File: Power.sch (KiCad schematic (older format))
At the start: 29 parts

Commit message: Clean up, add notes
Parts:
- added C?: 1u, symbol Device:C
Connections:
- net +5V: now also C?.1
- net GND: now also C?.2
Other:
- note added: "6 months sleep: 6*30*24h * (30e-3)mA = 130mAh\n3 days run: 3*24h * 10mA = 720mAh\n\nTotal: 850mAh\nEst. True Total: 500mAh"
- note added: "PS: Pull low for power save mode\nand pull high for fixed switching \nfrequency operation. \n\nEfficiency:\n85% @ 1-3mA PSM\n25% @ 1-3mA FFM\n"
- note added: "Power Consumption Rough Max Estimates"
- note added: "Shutdown Iq: 0.1uA typ, 1uA max\nRun efficiency: 85% (-0.5mA res div)"
- note added: "Shutdown Iq: 0.2uA typ, 1uA max\nRun Iq: 250uA typ, 425uA max @ 250mA"
- note added: "Sleep Total Iq: \n(2+1+7+1.2+10)uA/85% + 5uA = 30uA max\n\nSensor/Comm Duty Cycle:\n15s/(10*60s) = 2.5%\n\nRun Total:\n3.3V: [3.3mA + (2.5%)(2.6+5+0.5+0.5)mA]/85% = 5mA max\n5.0V: (2.5%)(100+0.5)mA/85% = 3mA max -> 5mA @ 3.3V"
- note removed: "PS: Pull low for power save mode\nand pull high for fixed switching \nfrequency operation."
- note removed: "Shutdown Iq: 0.1uA typ, 1uA max"
- moved on the sheet: C?, D?, J?, L?, R?, U?

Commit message: Cleanup
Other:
- note removed: "6 months sleep: 6*30*24h * (30e-3)mA = 130mAh\n3 days run: 3*24h * 10mA = 720mAh\n\nTotal: 850mAh\nEst. True Total: 500mAh"
- note removed: "Power Consumption Rough Max Estimates"
- note removed: "Sleep Total Iq: \n(2+1+7+1.2+10)uA/85% + 5uA = 30uA max\n\nSensor/Comm Duty Cycle:\n15s/(10*60s) = 2.5%\n\nRun Total:\n3.3V: [3.3mA + (2.5%)(2.6+5+0.5+0.5)mA]/85% = 5mA max\n5.0V: (2.5%)(100+0.5)mA/85% = 3mA max -> 5mA @ 3.3V"
- moved on the sheet: C?, D?, J?, L?, R?, U?

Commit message: Select caps
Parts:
- C? (x3): footprint (none) -> JetkovKiCADLib:C_0402_NoSilk; Description (none) -> CAP CER 1UF 10V X5R 0402; Manufacturer (none) -> Samsung Electro-Mechanics; Part Number (none) -> CL05A105KP5NNNC; Temp Range (none) -> -55°C +85°C
- C? (x2): footprint (none) -> JetkovKiCADLib:C_0603; Description (none) -> CAP CER 10UF 10V X5R 0603; Manufacturer (none) -> Samsung Electro-Mechanics; Part Number (none) -> CL10A106MP8NNNC; Temp Range (none) -> -55°C +85°C
- C? (x2): footprint (none) -> JetkovKiCADLib:C_0402_NoSilk; Description (none) -> CAP CER 4.7UF 10V X5R 0402; Manufacturer (none) -> Samsung Electro-Mechanics; Part Number (none) -> CL05A475MP5NRNC; Temp Range (none) -> -55°C +85°C
- C? (x2): footprint (none) -> JetkovKiCADLib:C_0603; Description (none) -> CAP CER 22UF 10V X5R 0603; Manufacturer (none) -> Murata Electronics; Part Number (none) -> GRM188R61A226ME15D; Temp Range (none) -> -55°C +85°C
- R? (x12): footprint (none) -> JetkovKiCADLib:R_0402_NoSilk
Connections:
- net LVR_FB: now reaches R?.1, R?.2, U?.10 (FB)
- net LVR_LX1: now reaches L?.1, U?.4 (LX1)
- net LVR_LX2: now reaches L?.2, U?.2 (LX2)
- net CST: now reaches R?.2, U?.1 (STAT)
- net CPR: now reaches R?.1, U?.5 (PROG)
- net HVR_SW: now reaches D?.2 (A), L?.2, U?.1 (SW)
- net HVR_FB: now reaches R?.1, R?.2, U?.3 (FB)
- net USB_CC2: now reaches J?.B5 (CC2), R?.1
- net USB_CC1: now reaches J?.A5 (CC1), R?.1
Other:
- moved on the sheet: C?, R?, U?

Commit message: cleanup, add inductors
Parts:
- L?: footprint (none) -> JetkovKiCADLib:MAMK2520T2R2M; Description (none) -> FIXED IND 2.2UH 1.9A 117 MOHM; Manufacturer (none) -> Taiyo Yuden; Part Number (none) -> MAMK2520T2R2M; Temp Range (none) -> -40°C +105°C
- L?: footprint (none) -> JetkovKiCADLib:LQH3NPZ4R7MMEL; Description (none) -> FIXED IND 4.7UH 1A 120 MOHM SMD; Manufacturer (none) -> Murata Electronics; Part Number (none) -> LQH3NPZ4R7MMEL; Temp Range (none) -> -40°C +105°C
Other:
- note added: "PP / VBUS"
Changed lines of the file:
@@
 F 0 "L?" V 3985 3401 50  0000 C CNN
 F 1 "2.2u" V 3842 3401 50  0000 C CNN
-F 2 "" H 3900 3400 50  0001 C CNN
-F 3 "~" H 3900 3400 50  0001 C CNN
+F 2 "JetkovKiCADLib:MAMK2520T2R2M" H 3900 3400 50  0001 C CNN
+F 3 "https://ds.yuden.co.jp/TYCOMPAS/ut/detail?pn=MAMK2520T2R2M%20%20&u=M" H 3900 3400 50  0001 C CNN
+F 4 "FIXED IND 2.2UH 1.9A 117 MOHM" H 3900 3400 50  0001 C CNN "Description"
+F 5 "Taiyo Yuden" H 3900 3400 50  0001 C CNN "Manufacturer"
+F 6 "MAMK2520T2R2M" H 3900 3400 50  0001 C CNN "Part Number"
+F 7 "-40°C +105°C" H 3900 3400 50  0001 C CNN "Temp Range"
 	1    3900 3400
 	0    -1   -1   0
@@
 F 0 "L?" V 6900 3500 50  0000 C CNN
 F 1 "4.7u" V 6728 3497 50  0000 C CNN
-F 2 "" H 6800 3500 50  0001 C CNN
-F 3 "~" H 6800 3500 50  0001 C CNN
+F 2 "JetkovKiCADLib:LQH3NPZ4R7MMEL" H 6800 3500 50  0001 C CNN
+F 3 "https://search.murata.co.jp/Ceramy/image/img/P02/JELF243A-9140.pdf" H 6800 3500 50  0001 C CNN
+F 4 "FIXED IND 4.7UH 1A 120 MOHM SMD" H 6800 3500 50  0001 C CNN "Description"
+F 5 "Murata Electronics" H 6800 3500 50  0001 C CNN "Manufacturer"
+F 6 "LQH3NPZ4R7MMEL" H 6800 3500 50  0001 C CNN "Part Number"
+F 7 "-40°C +105°C" H 6800 3500 50  0001 C CNN "Temp Range"
 	1    6800 3500
 	0    -1   -1   0
@@
 Text Notes 6350 3200 0    79   ~ 0
 Boost Converter
-Connection ~ 6350 4200
-$Comp
-L JetkovKiCADLib:MIC2288YD5 U?
-U 1 1 60683D0E
-P 6800 4000
-F 0 "U?" H 6600 4350 50  0000 C CNN
-F 1 "MIC2288YD5" H 6772 3545 50  0000 C CNN
-F 2 "JetkovKiCADLib:MIC2288YD5" H 6550 3400 50  0001 L BNN
-F 3 "http://www.microchip.com/mymicrochip/filehandler.aspx?ddocname=en580187" H 7100 3550 50  0001 L BNN
-F 4 "MIC2288YD5-TR" H 6850 3300 40  0001 C CNN "Part Number"
-F 5 "Microchip Technology" H 6850 3300 40  0001 C CNN "Manufacturer"
-F 6 "IC REG BOOST ADJ 1.2A TSOT23-5" H 6850 3300 40  0001 C CNN "Description"
-F 7 "-40°C +125°C" H 6850 3300 40  0001 C CNN "Temp Range"
-	1    6800 4000
-	1    0    0    -1
-$EndComp
 Connection ~ 8050 3500
 $Comp
@@
 Wire Wire Line
 	5200 1350 5700 1350
+Connection ~ 6350 4200
+$Comp
+L JetkovKiCADLib:MIC2288YD5 U?
+U 1 1 60683D0E
+P 6800 4000
+F 0 "U?" H 6600 4350 50  0000 C CNN
+F 1 "MIC2288YD5" H 6772 3545 50  0000 C CNN
+F 2 "JetkovKiCADLib:MIC2288YD5" H 6550 3400 50  0001 L BNN
+F 3 "http://www.microchip.com/mymicrochip/filehandler.aspx?ddocname=en580187" H 7100 3550 50  0001 L BNN
+F 4 "MIC2288YD5-TR" H 6850 3300 40  0001 C CNN "Part Number"
+F 5 "Microchip Technology" H 6850 3300 40  0001 C CNN "Manufacturer"
+F 6 "IC REG BOOST ADJ 1.2A TSOT23-5" H 6850 3300 40  0001 C CNN "Description"
+F 7 "-40°C +125°C" H 6850 3300 40  0001 C CNN "Temp Range"
+	1    6800 4000
+	1    0    0    -1
+$EndComp
+Text Notes 4800 2350 0    40   ~ 0
+PP / VBUS
 $EndSCHEMATC

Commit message: Add diode info
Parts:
- D?: footprint (none) -> JetkovKiCADLib:PMEG2010EA; Description (none) -> DIODE SCHOTTKY 20V 1A SOD323; Manufacturer (none) -> Nexperia USA Inc.; Part Number (none) -> PMEG2010EA,135; Temp Range (none) -> -65°C +125°C
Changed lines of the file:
@@
 F 0 "D?" H 7450 3375 50  0000 C CNN
 F 1 "D_Schottky" H 7450 3374 50  0001 C CNN
-F 2 "" H 7450 3500 50  0001 C CNN
-F 3 "~" H 7450 3500 50  0001 C CNN
+F 2 "JetkovKiCADLib:PMEG2010EA" H 7450 3500 50  0001 C CNN
+F 3 "https://assets.nexperia.com/documents/data-sheet/PMEG2010EA.pdf" H 7450 3500 50  0001 C CNN
+F 4 "DIODE SCHOTTKY 20V 1A SOD323" H 7450 3500 50  0001 C CNN "Description"
+F 5 "Nexperia USA Inc." H 7450 3500 50  0001 C CNN "Manufacturer"
+F 6 "PMEG2010EA,135" H 7450 3500 50  0001 C CNN "Part Number"
+F 7 "-65°C +125°C" H 7450 3500 50  0001 C CNN "Temp Range"
 	1    7450 3500
 	-1   0    0    1

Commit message: Fix part info, start rough layout
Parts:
- gave numbers to parts that had none: 30

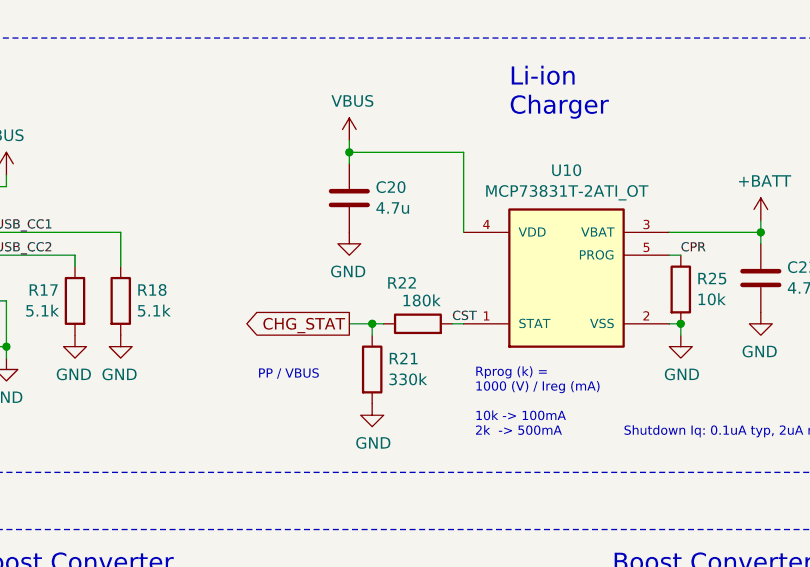
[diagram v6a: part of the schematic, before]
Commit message: Clean up schem, wire in button
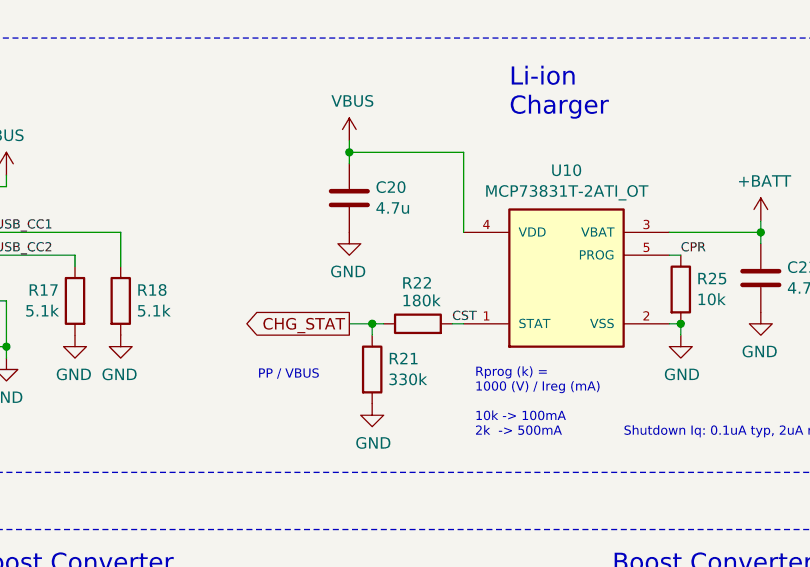
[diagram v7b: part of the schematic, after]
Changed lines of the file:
@@
 U 1 1 60683DB5
 P 5500 2100
-F 0 "R22" V 5677 2102 50  0000 L CNN
+F 0 "R22" V 5677 2036 50  0000 L CNN
 F 1 "180k" V 5600 2000 50  0000 L CNN
 F 2 "JetkovKiCADLib:R_0402_NoSilk" V 5430 2100 50  0001 C CNN

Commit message: Review
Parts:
- R21: value 330k -> 300k
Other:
- note added: "5.2V -> 3.25V"
- note removed: "PP / VBUS"
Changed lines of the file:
@@
 P 5300 2300
 F 0 "R21" H 5370 2346 50  0000 L CNN
-F 1 "330k" H 5370 2255 50  0000 L CNN
+F 1 "300k" H 5370 2255 50  0000 L CNN
 F 2 "JetkovKiCADLib:R_0402_NoSilk" V 5230 2300 50  0001 C CNN
 F 3 "~" H 5300 2300 50  0001 C CNN
@@
 	1    0    0    -1
 $EndComp
-Text Notes 4800 2350 0    40   ~ 0
-PP / VBUS
+Text Notes 4700 2350 0    40   ~ 0
+5.2V -> 3.25V
 $EndSCHEMATC
